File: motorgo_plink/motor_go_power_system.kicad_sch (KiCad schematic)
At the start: 35 parts, among them J1 USB4520-03-0-A_REVA, Q1 SI2323, U6 TPS54620RHLR, U7 HUSB238_002DD, U8 AMS1117-3.3

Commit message: updated BOM in prep for order - TS
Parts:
- D4: LCSC_Part_Number (none) -> C5366311
- J1: LCSC_Part_Number C2965608 -> C720628
- L1: LCSC_Part_Number (none) -> C2847540
- Q1: LCSC_Part_Number (none) -> C5278892
- R16: LCSC_Part_Number (none) -> C2933066
- R17: LCSC_Part_Number (none) -> C25887
- R18: LCSC_Part_Number (none) -> C5153961
- R19: LCSC_Part_Number (none) -> C3013164
- R20: LCSC_Part_Number (none) -> C2906862
- R23: LCSC_Part_Number (none) -> C409700
- R24: LCSC_Part_Number (none) -> C2998086
- R25, R27: LCSC_Part_Number (none) -> C2906885
- R26: LCSC_Part_Number (none) -> C2906873
- R28: LCSC_Part_Number (none) -> C3015834
- R29: LCSC_Part_Number (none) -> C3013149
- U6: LCSC_Part_Number (none) -> C263274
- U7: LCSC_Part_Number (none) -> C7471904
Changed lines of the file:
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@@
       (effects (font (size 1.27 1.27)) hide)
     )
-    (property "Datasheet" "~" (at 79.375 99.06 0)
+    (property "Datasheet" "https://www.lcsc.com/product-detail/Chip-Resistor-Surface-Mount_FOJAN-FRC0402F3401TS_C3013164.html" (at 79.375 99.06 0)
+      (effects (font (size 1.27 1.27)) hide)
+    )
+    (property "LCSC_Part_Number" "C3013164" (at 79.375 99.06 0)
       (effects (font (size 1.27 1.27)) hide)
     )
@@
       (effects (font (size 1.27 1.27)) hide)
     )
-    (property "Datasheet" "" (at 120.015 145.9738 0)
+    (property "Datasheet" "https://www.lcsc.com/product-detail/span-style-background-color-ff0-USB-span-Converters_Hynetek-HUSB238_002DD_C7471904.html" (at 120.015 145.9738 0)
       (effects (font (size 1.27 1.27)) hide)
     )
@@
     )
     (property "uuid" "std:72c35b3c087241289ee1276473b7df23" (at 120.015 151.0538 0)
+      (effects (font (size 1.27 1.27)) hide)
+    )
+    (property "LCSC_Part_Number" "C7471904" (at 120.015 146.05 0)
       (effects (font (size 1.27 1.27)) hide)
     )
@@
       (effects (font (size 1.27 1.27)) hide)
     )
-    (property "Datasheet" "~" (at 104.775 135.89 0)
+    (property "Datasheet" "https://www.lcsc.com/product-detail/Chip-Resistor-Surface-Mount_FOJAN-FRC0402F10R0TS_C2906862.html" (at 104.775 135.89 0)
+      (effects (font (size 1.27 1.27)) hide)
+    )
+    (property "LCSC_Part_Number" "C2906862" (at 104.775 135.89 0)
       (effects (font (size 1.27 1.27)) hide)
     )
@@
       (effects (font (size 1.27 1.27)) hide)
     )
-    (property "Datasheet" "~" (at 152.4 133.985 0)
+    (property "Datasheet" "https://www.lcsc.com/product-detail/MOSFETs_PAKER-SI2323_C5278892.html" (at 152.4 133.985 0)
+      (effects (font (size 1.27 1.27)) hide)
+    )
+    (property "LCSC_Part_Number" "C5278892" (at 152.4 133.985 0)
       (effects (font (size 1.27 1.27)) hide)
     )
@@
       (effects (font (size 1.27 1.27)) hide)
     )
-    (property "Datasheet" "~" (at 138.43 140.97 0)
+    (property "Datasheet" "https://www.lcsc.com/product-detail/Chip-Resistor-Surface-Mount_Viking-Tech-CR-02FL6-5K1_C409700.html" (at 138.43 140.97 0)
+      (effects (font (size 1.27 1.27)) hide)
+    )
+    (property "LCSC_Part_Number" "C409700" (at 138.43 140.97 0)
       (effects (font (size 1.27 1.27)) hide)
     )
@@
       (effects (font (size 1 1)) (justify bottom) hide)
     )
-    (property "Datasheet" "" (at 194.945 118.11 0)
+    (property "Datasheet" "https://www.lcsc.com/product-detail/USB-Connectors_XUNPU-TYPEC-303-ACP16_C720628.html" (at 194.945 118.11 0)
       (effects (font (size 1.27 1.27)) hide)
     )
@@
       (effects (font (size 1.27 1.27)) (justify bottom) hide)
     )
-    (property "LCSC_Part_Number" "C2965608" (at 194.945 118.11 0)
+    (property "LCSC_Part_Number" "C720628" (at 194.945 118.11 0)
       (effects (font (size 1.27 1.27)) hide)
     )
@@
       (effects (font (size 1.27 1.27)) hide)
     )
-    (property "Datasheet" "~" (at 73.66 99.06 0)
+    (property "Datasheet" "https://www.lcsc.com/product-detail/Chip-Resistor-Surface-Mount_FOJAN-FRC0402F5362TS_C5153961.html" (at 73.66 99.06 0)
+      (effects (font (size 1.27 1.27)) hide)
+    )
+    (property "LCSC_Part_Number" "C5153961" (at 73.66 99.06 0)
       (effects (font (size 1.27 1.27)) hide)
     )
@@
       (effects (font (size 1.27 1.27)) hide)
     )
-    (property "Datasheet" "~" (at 111.76 131.445 0)
+    (property "Datasheet" "https://www.lcsc.com/product-detail/Schottky-Barrier-Diodes-SBD_Shikues-SS52BF_C5366311.html" (at 111.76 131.445 0)
+      (effects (font (size 1.27 1.27)) hide)
+    )
+    (property "LCSC_Part_Number" "C5366311" (at 111.76 131.445 0)
       (effects (font (size 1.27 1.27)) hide)
     )
@@
       (effects (font (size 1.27 1.27)) hide)
     )
-    (property "Datasheet" "~" (at 142.875 71.755 0)
+    (property "Datasheet" "https://www.lcsc.com/product-detail/Chip-Resistor-Surface-Mount_FOJAN-FRC0402F5232TS_C2998086.html" (at 142.875 71.755 0)
+      (effects (font (size 1.27 1.27)) hide)
+    )
+    (property "LCSC_Part_Number" "C2998086" (at 142.875 71.755 0)
       (effects (font (size 1.27 1.27)) hide)
     )
@@
       (effects (font (size 1.27 1.27)) hide)
     )
-    (property "Datasheet" "~" (at 146.685 169.545 0)
+    (property "Datasheet" "https://www.lcsc.com/product-detail/Chip-Resistor-Surface-Mount_FOJAN-FRC0402J103-TS_C2906885.html" (at 146.685 169.545 0)
+      (effects (font (size 1.27 1.27)) hide)
+    )
+    (property "LCSC_Part_Number" "C2906885" (at 146.685 169.545 0)
       (effects (font (size 1.27 1.27)) hide)
     )
@@
       (effects (font (size 1.27 1.27)) hide)
     )
-    (property "Datasheet" "~" (at 60.96 86.36 0)
+    (property "Datasheet" "https://www.lcsc.com/product-detail/Chip-Resistor-Surface-Mount_UNI-ROYAL-Uniroyal-Elec-0402WGF3652TCE_C25887.html" (at 60.96 86.36 0)
+      (effects (font (size 1.27 1.27)) hide)
+    )
+    (property "LCSC_Part_Number" "C25887" (at 60.96 86.36 0)
       (effects (font (size 1.27 1.27)) hide)
     )
@@
       (effects (font (size 1.27 1.27)) hide)
     )
-    (property "Datasheet" "~" (at 134.62 65.405 0)
+    (property "Datasheet" "https://www.lcsc.com/product-detail/Inductors-SMD_KOHERelec-MDA7050-3R3M_C2847540.html" (at 134.62 65.405 0)
+      (effects (font (size 1.27 1.27)) hide)
+    )
+    (property "LCSC_Part_Number" "C2847540" (at 134.62 65.405 0)
       (effects (font (size 1.27 1.27)) hide)
     )
@@
       (effects (font (size 1.27 1.27)) hide)
     )
-    (property "Datasheet" "~" (at 145.415 136.525 0)
+    (property "Datasheet" "https://www.lcsc.com/product-detail/Chip-Resistor-Surface-Mount_FOJAN-FRC0402F4992TS_C2906873.html" (at 145.415 136.525 0)
+      (effects (font (size 1.27 1.27)) hide)
+    )
+    (property "LCSC_Part_Number" "C2906873" (at 145.415 136.525 0)
       (effects (font (size 1.27 1.27)) hide)
     )
@@
       (effects (font (size 1.27 1.27)) hide)
     )
-    (property "Datasheet" "http://www.szlcsc.com/product/details_254511.html" (at 97.79 70.4088 0)
+    (property "Datasheet" "https://www.lcsc.com/product-detail/DC-DC-Converters_Texas-Instruments-TPS54620RHLR_C263274.html" (at 97.79 70.4088 0)
       (effects (font (size 1.27 1.27)) hide)
     )
@@
     )
     (property "uuid" "std:22c093bd3f0e4f169efe6636adc161b3" (at 97.79 75.4888 0)
+      (effects (font (size 1.27 1.27)) hide)
+    )
+    (property "LCSC_Part_Number" "C263274" (at 97.79 80.645 0)
       (effects (font (size 1.27 1.27)) hide)
     )
@@
       (effects (font (size 1.27 1.27)) hide)
     )
-    (property "Datasheet" "~" (at 159.385 168.91 0)
+    (property "Datasheet" "https://www.lcsc.com/product-detail/Chip-Resistor-Surface-Mount_FOJAN-FRC0402F1052TS_C3013149.html" (at 159.385 168.91 0)
+      (effects (font (size 1.27 1.27)) hide)
+    )
+    (property "LCSC_Part_Number" "C3013149" (at 159.385 168.91 0)
       (effects (font (size 1.27 1.27)) hide)
     )
@@
       (effects (font (size 1.27 1.27)) hide)
     )
-    (property "Datasheet" "~" (at 142.875 87.63 0)
+    (property "Datasheet" "https://www.lcsc.com/product-detail/Chip-Resistor-Surface-Mount_FOJAN-FRC0402J103-TS_C2906885.html" (at 142.875 87.63 0)
+      (effects (font (size 1.27 1.27)) hide)
+    )
+    (property "LCSC_Part_Number" "C2906885" (at 142.875 87.63 0)
       (effects (font (size 1.27 1.27)) hide)
     )
@@
       (effects (font (size 1.27 1.27)) hide)
     )
-    (property "Datasheet" "~" (at 60.96 75.565 0)
+    (property "Datasheet" "https://www.lcsc.com/product-detail/Chip-Resistor-Surface-Mount_FOJAN-FRC0402F1023TS_C2933066.html" (at 60.96 75.565 0)
+      (effects (font (size 1.27 1.27)) hide)
+    )
+    (property "LCSC_Part_Number" "C2933066" (at 60.96 75.565 0)
       (effects (font (size 1.27 1.27)) hide)
     )
@@
       (effects (font (size 1.27 1.27)) hide)
     )
-    (property "Datasheet" "~" (at 150.495 169.545 0)
-      (effects (font (size 1.27 1.27)) hide)
-    )
+    (property "Datasheet" "https://www.lcsc.com/product-detail/Chip-Resistor-Surface-Mount_VO-SCR0402F14K_C3015834.html" (at 150.495 169.545 0)
+      (effects (font (size 1.27 1.27)) hide)
+    )
+    (property "LCSC_Part_Number" "C3015834" (at 150.495 169.545 0)
+      (effects (font (size 1.27 1.27)) hide)
+    )

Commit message: added J11 p/n - TS
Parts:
- J8: LCSC_Part_Number - -> C319099
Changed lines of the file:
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@@
       (effects (font (size 1.27 1.27)) hide)
     )
-    (property "Datasheet" "" (at 44.45 146.05 0)
-      (effects (font (size 1.27 1.27)) hide)
-    )
-    (property "LCSC_Part_Number" "-" (at 43.815 146.685 0)
+    (property "Datasheet" "https://www.lcsc.com/product-detail/DC-Power-Connector_XKB-Connection-DC-005-2-5A-2-0_C319099.html" (at 44.45 146.05 0)
+      (effects (font (size 1.27 1.27)) hide)
+    )
+    (property "LCSC_Part_Number" "C319099" (at 43.815 146.685 0)
       (effects (font (size 1.27 1.27)) hide)
     )
@@
       (effects (font (size 1.27 1.27)) hide)
     )
-    (property "Datasheet" "http://www.advanced-monolithic.com/pdf/ds1117.pdf" (at 198.12 65.405 0)
-      (effects (font (size 1.27 1.27)) hide)
-    )
+    (property "Datasheet" "https://www.lcsc.com/product-detail/Linear-Voltage-Regulators-LDO_UMW-Youtai-Semiconductor-Co-Ltd-AMS1117-3-3_C347222.html" (at 198.12 65.405 0)
+      (effects (font (size 1.27 1.27)) hide)
+    )

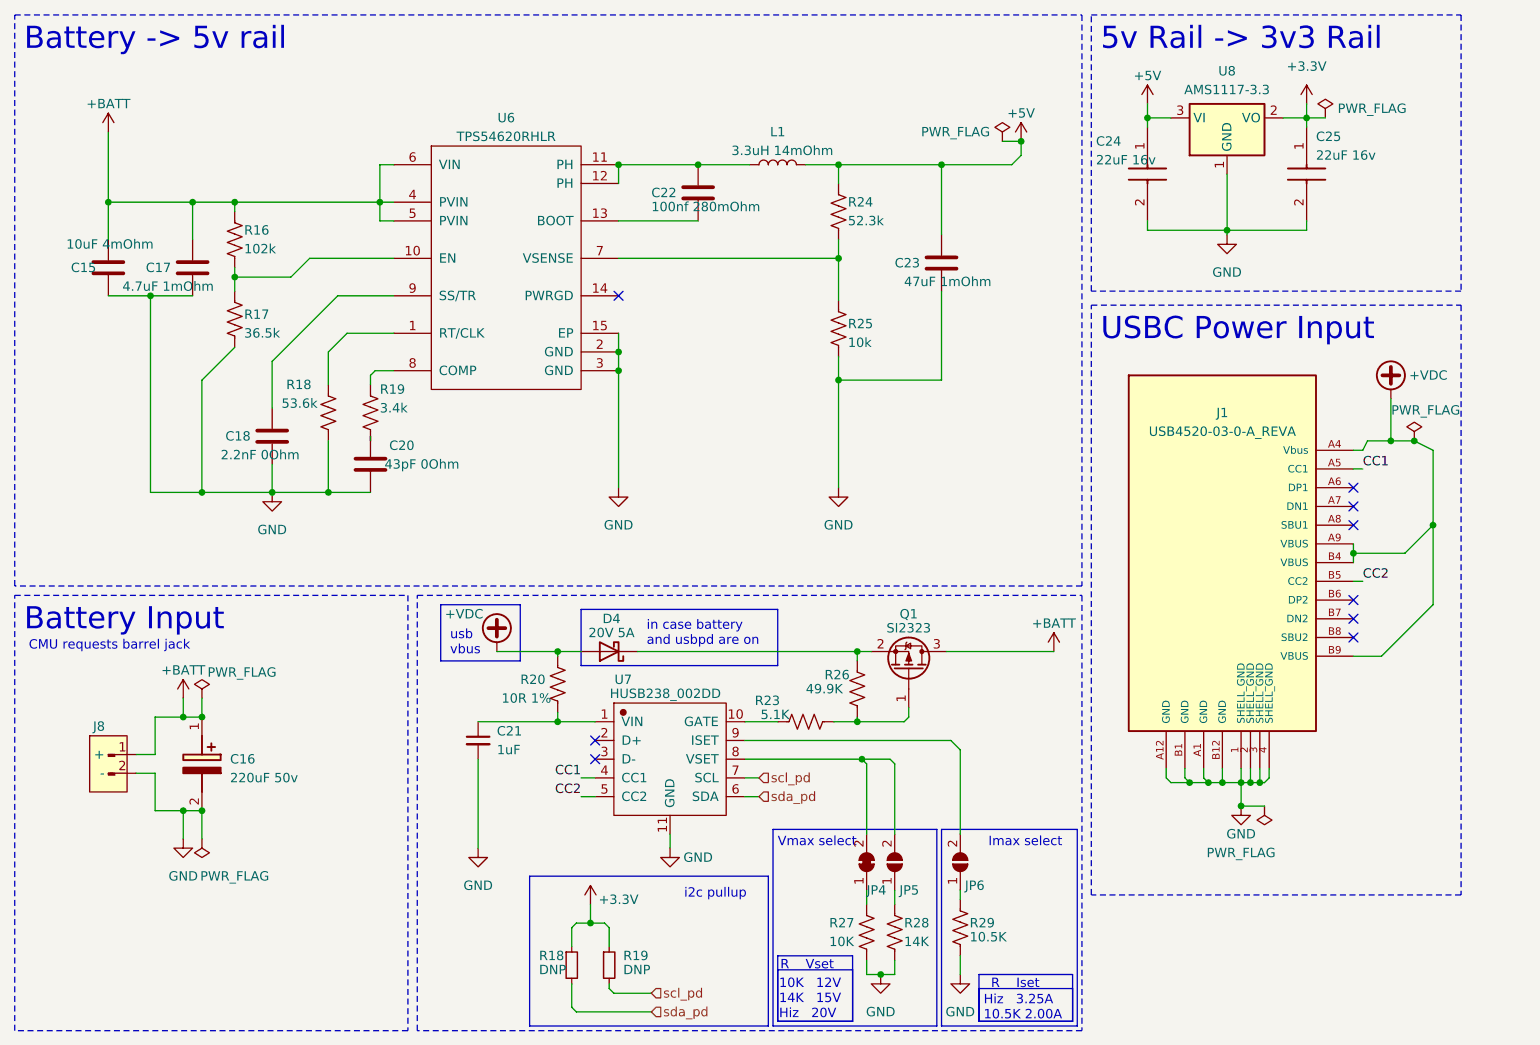
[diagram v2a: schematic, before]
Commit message: wip culling of non-vital schematic components
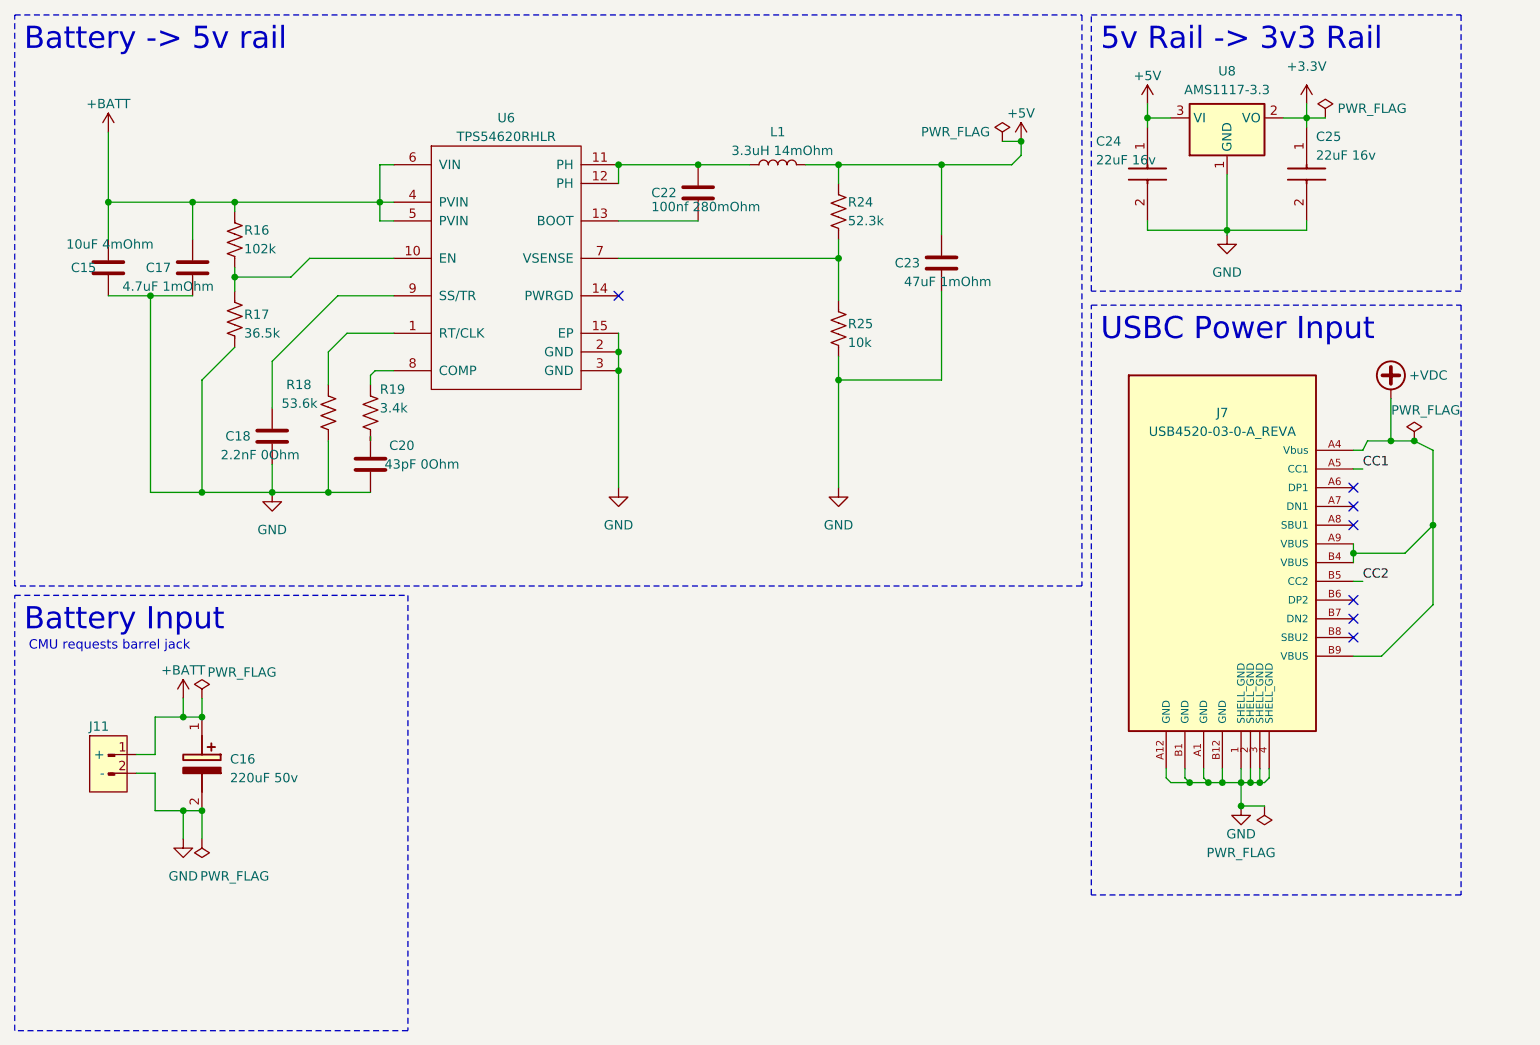
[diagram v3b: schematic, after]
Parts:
- removed C21: 1uF, Capacitor_SMD:C_0603_1608Metric, symbol Device:C_Small
- removed D4: 20V 5A, LCSC_parts:D_SMB_LCSC_C5366311, symbol Device:D_Schottky
- removed JP4: SolderJumper_2_Bridged, Jumper:SolderJumper-2_P1.3mm_Bridged2Bar_RoundedPad1.0x1.5mm, symbol Jumper:SolderJumper_2_Bridged
- removed JP5, JP6: SolderJumper_2_Open, Jumper:SolderJumper-2_P1.3mm_Open_RoundedPad1.0x1.5mm, symbol Jumper:SolderJumper_2_Open
- removed Q1: SI2323, LCSC_parts:SI2323_SOT-23-3_L2.9-W1.3-P0.95-LS2.4-BR, symbol Device:Q_PMOS_GSD
- removed R18, R19: DNP, Resistor_SMD:R_0402_1005Metric, symbol Device:R_Small
- removed R20: 10R 1%, Resistor_SMD:R_0402_1005Metric, symbol Device:R_US
- removed R23: 5.1K, Resistor_SMD:R_0402_1005Metric, symbol Device:R_US
- removed R26: 49.9K, Resistor_SMD:R_0402_1005Metric, symbol Device:R_US
- removed R27: 10K, Resistor_SMD:R_0402_1005Metric, symbol Device:R_US
- removed R28: 14K, Resistor_SMD:R_0402_1005Metric, symbol Device:R_US
- removed R29: 10.5K, Resistor_SMD:R_0402_1005Metric, symbol Device:R_US
- removed U7: HUSB238_002DD, LCSC_parts:DFN-10_L3.0-W3.0-P0.50-BL-EP2.5, symbol LCSC_imports:HUSB238_002DD
- renumbered J8 to J11, J1 to J7
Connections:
- no-connect marks 9 -> 7
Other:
- note removed: "10K 12V 14K 15V Hiz 20V"
- note removed: "Hiz 3.25A 10.5K 2.00A"
- note removed: "Imax select"
- note removed: "R Iset"
- note removed: "R Vset"
- note removed: "Vmax select"
- note removed: "i2c pullup"
- note removed: "in case battery and usbpd are on"
- note removed: "usb vbus"
